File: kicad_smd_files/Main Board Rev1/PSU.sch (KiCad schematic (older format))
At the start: 30 parts, among them IC1 LD1086BDTTR, IC2 L7805CV, IC3 L7809ABV, IC4 L7809ABV, J1 Barrel_Jack_MountingPin, J2 +12V Battery

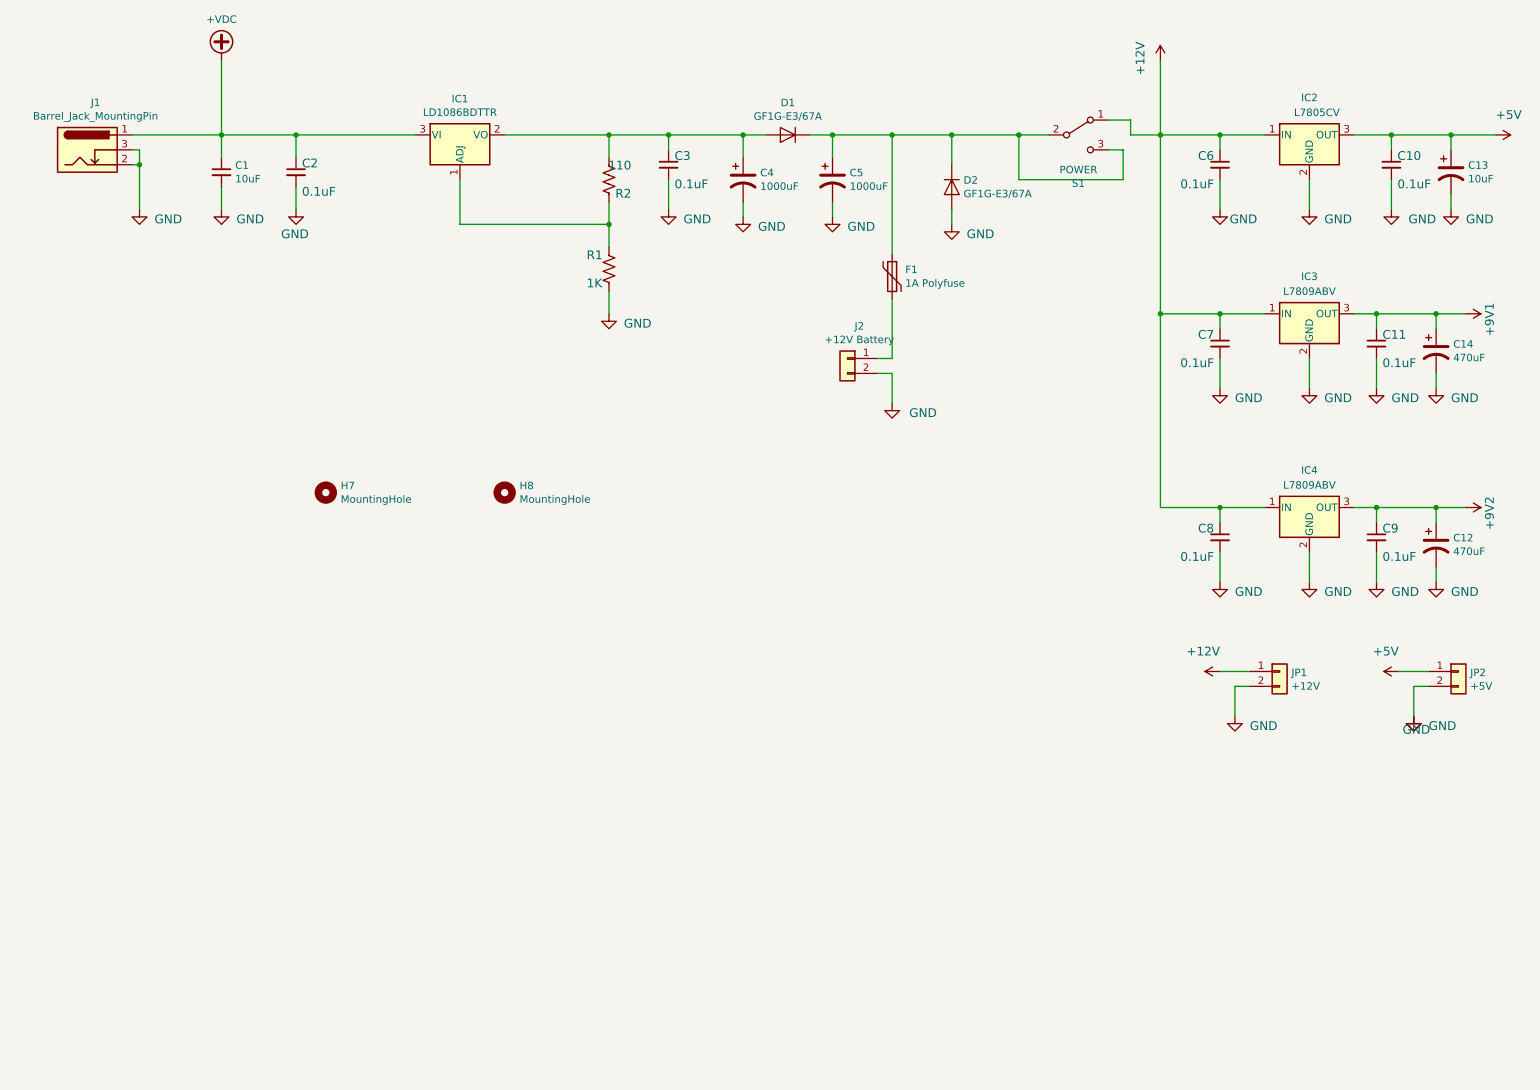
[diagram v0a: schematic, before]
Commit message: Firmware patch to support new LCD, more beefy power circuit for LiPo, added LiPo Balance and protection, fixed reversed op-amp comparitor pins
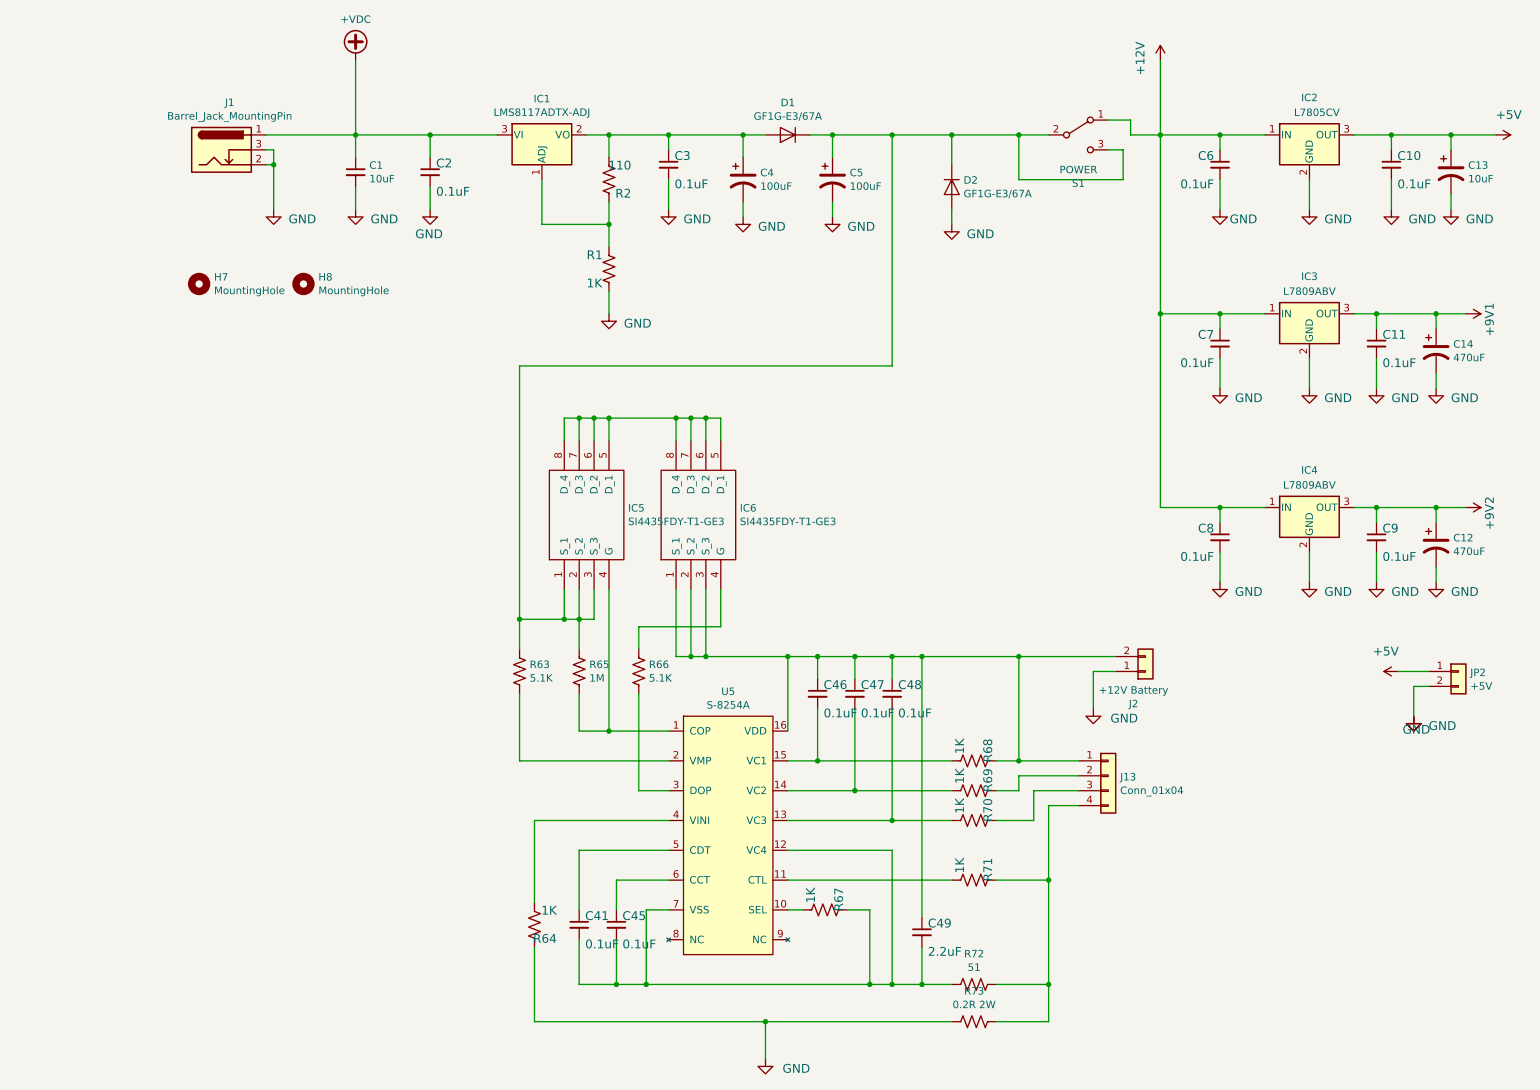
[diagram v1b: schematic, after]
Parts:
- removed F1: 1A Polyfuse, Fuse:Fuse_2920_7451Metric, symbol Device:Polyfuse
- removed JP1: +12V, Connector_PinHeader_2.54mm:PinHeader_1x02_P2.54mm_Vertical, symbol Connector_Generic:Conn_01x02
- added C41, C45, C46, C47, C48: 0.1uF, Capacitor_SMD:C_0402_1005Metric, symbol Device:C_Small
- added C49: 2.2uF, Capacitor_SMD:C_0603_1608Metric, symbol Device:C_Small
- added IC5, IC6: SI4435FDY-T1-GE3, mk312-smd-footprints:SOIC127P600X175-8N, symbol SamacSys_Parts:SI4435FDY-T1-GE3
- added J13: Conn_01x04, Connector_JST:JST_XH_B4B-XH-A_1x04_P2.50mm_Vertical, symbol Connector_Generic:Conn_01x04
- added R63, R66: 5.1K, Resistor_SMD:R_0603_1608Metric, symbol Device:R_US
- added R64, R67, R68, R69, R70, R71: 1K, Resistor_SMD:R_0603_1608Metric, symbol Device:R_US
- added R65: 1M, Resistor_SMD:R_0603_1608Metric, symbol Device:R_US
- added R72: 51, Resistor_SMD:R_0603_1608Metric, symbol Device:R_US
- added R73: 0.2R 2W, Resistor_SMD:R_2512_6332Metric, symbol Device:R_US
- added U5: S-8254A, Package_SO:TSSOP-16_4.4x5mm_P0.65mm, symbol estim_parts:S-8254A
- C1: Manufacturer_Name Panasonic -> Taiyo Yuden; Manufacturer_Part_Number EEE-FK1C100R -> TMK212BBJ106MG-T; Mouser Part Number 667-EEE-FK1C100R -> 963-TMK212BBJ106MG-T
- C4, C5: value 1000uF -> 100uF; footprint Capacitor_SMD:C_Elec_10x10.2 -> Capacitor_SMD:C_Elec_6.3x7.7; Manufacturer_Part_Number EEE-FT1C102AP -> EEE-HC1C101XP; Mouser Part Number 667-EEE-FT1C102AP -> 667-EEE-HC1C101XP
- IC1: value LD1086BDTTR -> LMS8117ADTX-ADJ; Manufacturer_Name STMicroelectronics -> Texas Instruments; Manufacturer_Part_Number LD1086BDTTR -> LMS8117ADTX-ADJ; Mouser Part Number 511-LD1086BDTTR -> 926-LS8117ADTXADJNPB
- J2: footprint Connector_Wire:SolderWirePad_1x02_P3.81mm_Drill0.8mm -> Connector_AMASS:AMASS_XT30U-M_1x02_P5.0mm_Vertical
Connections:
- net GND: now also J2.1 (Pin_1), R64.1, R73.2; no longer J2.2 (Pin_2)
- net at C5.1, D1.1 (K), D2.1 (K)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: now also IC5.1 (S_1), IC5.2 (S_2), IC5.3 (S_3), R63.1, R65.1
- new net: IC5.4 (G), R65.2, U5.1 (COP)
- new net: R67.2, U5.10 (SEL)
- new net: R71.2, U5.11 (CTL)
- new net: C41.2, C45.2, C49.2, R67.1, R72.2, U5.12 (VC4), U5.7 (VSS)
- new net: C48.2, R70.2, U5.13 (VC3)
- new net: C47.2, R69.2, U5.14 (VC2)
- new net: C46.2, R68.2, U5.15 (VC1)
- new net: C46.1, C47.1, C48.1, C49.1, IC6.1 (S_1), IC6.2 (S_2), IC6.3 (S_3), J13.1 (Pin_1), J2.2 (Pin_2), R68.1, U5.16 (VDD)
- new net: R63.2, U5.2 (VMP)
- new net: R66.2, U5.3 (DOP)
- new net: R64.2, U5.4 (VINI)
- new net: C41.1, U5.5 (CDT)
- new net: C45.1, U5.6 (CCT)
- new net: IC5.5 (D_1), IC5.6 (D_2), IC5.7 (D_3), IC5.8 (D_4), IC6.5 (D_1), IC6.6 (D_2), IC6.7 (D_3), IC6.8 (D_4)
- new net: IC6.4 (G), R66.1
- new net: J13.2 (Pin_2), R69.1
- new net: J13.4 (Pin_4), R71.1, R72.1, R73.1
- new net: J13.3 (Pin_3), R70.1
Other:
- moved on the sheet: C1, C2, H7, H8, IC1, J1, J2
